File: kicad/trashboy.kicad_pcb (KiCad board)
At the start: 2 copper layers, 8 parts, among them J1 Conn_01x02, X1 TERMBLOCK_1X2

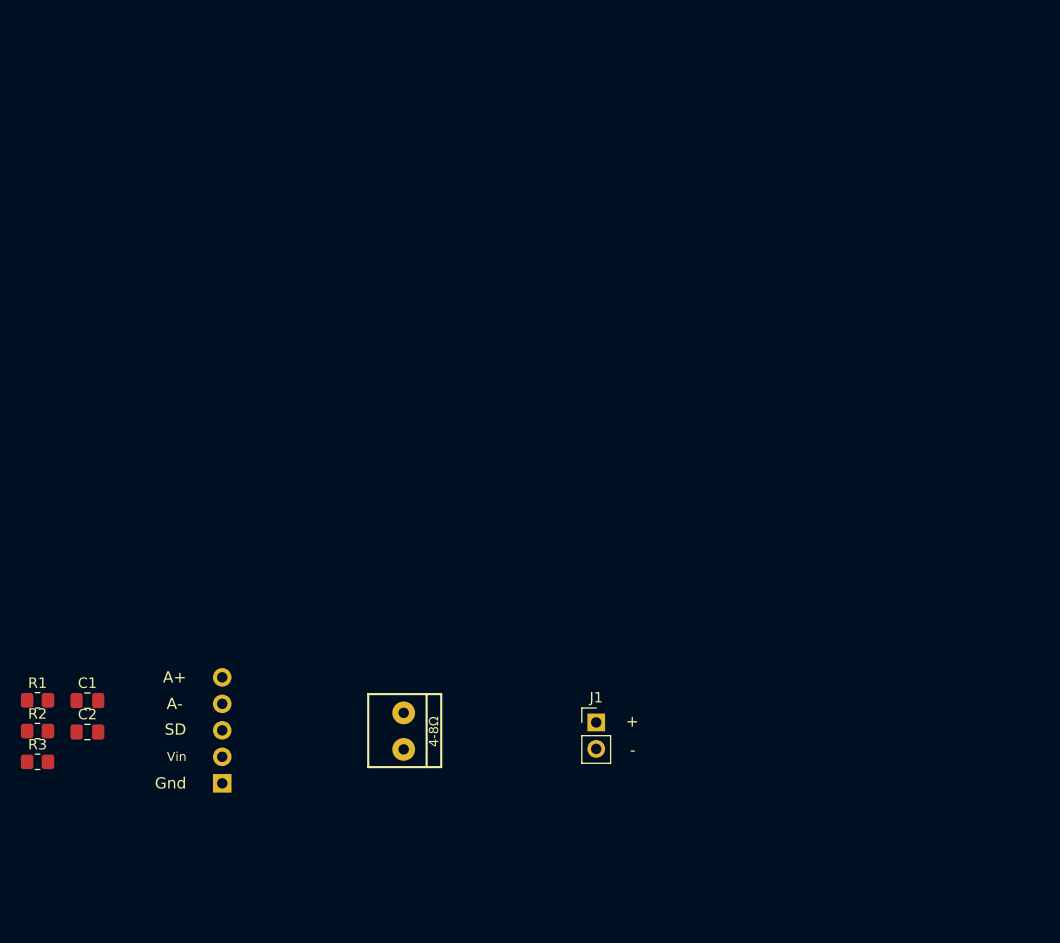
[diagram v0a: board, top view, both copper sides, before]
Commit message: Adding all of the component to the schematics.
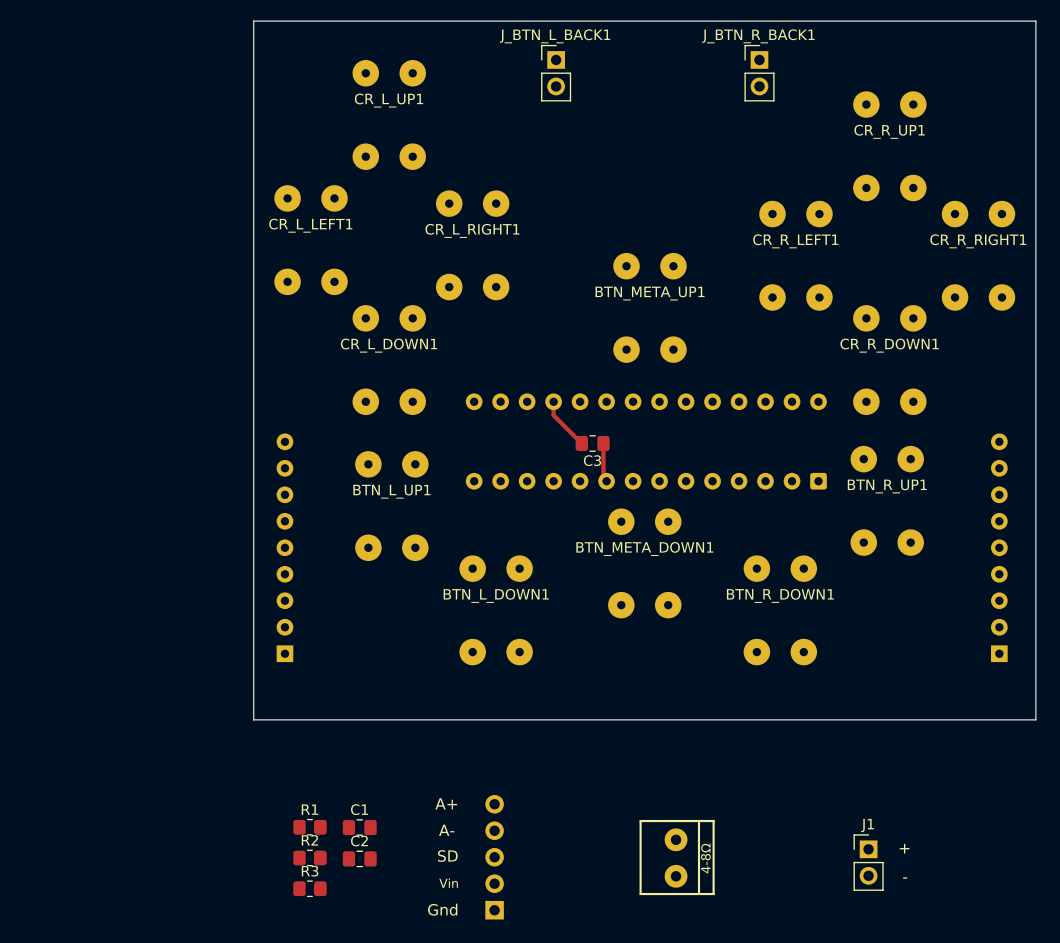
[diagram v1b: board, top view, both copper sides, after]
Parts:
- added BTN_L_DOWN1: SW_Push_Dual, buttons:SW_Push_Silicone_8x5mm, F.Cu at (165.8, 93.5)
- added BTN_L_UP1: SW_Push_Dual, buttons:SW_Push_Silicone_8x5mm, F.Cu at (155.8, 83.5)
- added BTN_META_DOWN1: SW_Push_Dual, buttons:SW_Push_Silicone_8x5mm, F.Cu at (180.0, 89.0)
- added BTN_META_UP1: SW_Push_Dual, buttons:SW_Push_Silicone_8x5mm, F.Cu at (180.5, 64.5)
- added BTN_R_DOWN1: SW_Push_Dual, buttons:SW_Push_Silicone_8x5mm, F.Cu at (193.0, 93.5)
- added BTN_R_UP1: SW_Push_Dual, buttons:SW_Push_Silicone_8x5mm, F.Cu at (203.2, 83.0)
- added C3: 10nF, Capacitor_SMD:C_0805_2012Metric_Pad1.18x1.45mm_HandSolder, F.Cu at (175.0, 77.5)
- added CR_L_DOWN1: SW_Push_Dual, buttons:SW_Push_Silicone_8x5mm, F.Cu at (155.5, 69.5)
- added CR_L_LEFT1: SW_Push_Dual, buttons:SW_Push_Silicone_8x5mm, F.Cu at (148.0, 58.0)
- added CR_L_RIGHT1: SW_Push_Dual, buttons:SW_Push_Silicone_8x5mm, F.Cu at (163.5, 58.5)
- added CR_L_UP1: SW_Push_Dual, buttons:SW_Push_Silicone_8x5mm, F.Cu at (155.5, 46.0)
- added CR_R_DOWN1: SW_Push_Dual, buttons:SW_Push_Silicone_8x5mm, F.Cu at (203.5, 69.5)
- added CR_R_LEFT1: SW_Push_Dual, buttons:SW_Push_Silicone_8x5mm, F.Cu at (194.5, 59.5)
- added CR_R_RIGHT1: SW_Push_Dual, buttons:SW_Push_Silicone_8x5mm, F.Cu at (212.0, 59.5)
- added CR_R_UP1: SW_Push_Dual, buttons:SW_Push_Silicone_8x5mm, F.Cu at (203.5, 49.0)
- added J_BTN_L_BACK1: Conn_01x02, Connector_PinHeader_2.54mm:PinHeader_1x02_P2.54mm_Vertical, F.Cu at (171.5, 40.7)
- added J_BTN_R_BACK1: Conn_01x02, Connector_PinHeader_2.54mm:PinHeader_1x02_P2.54mm_Vertical, F.Cu at (191.0, 40.7)
- added RN1: R_Network08_US, Resistor_THT:R_Array_SIP9, B.Cu at (145.5, 97.7)
- added RN2: R_Network08_US, Resistor_THT:R_Array_SIP9, B.Cu at (214.0, 97.7)
- added U1: MCP23017x-x-SP, Package_DIP:DIP-28_W7.62mm, B.Cu at (196.7, 81.1)
- moved J1 28.8 mm to (201.5, 116.4)
- moved C1 28.8 mm to (152.7, 114.3)
- moved C2 28.8 mm to (152.7, 117.3)
- moved JP1 28.8 mm to (165.6, 117.2)
- moved R1 28.8 mm to (147.9, 114.3)
- moved R2 28.8 mm to (147.9, 117.2)
- moved R3 28.8 mm to (147.9, 120.2)
- moved X1 28.8 mm to (183.0, 117.3)
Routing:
- net +3.3V: track 0.00 -> 5.12 mm
- net GND: track 0.00 -> 3.75 mm
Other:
- board outline added: 75 x 67 mm

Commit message: First attempt to place all the components, no traces yet.
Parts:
- added J3: Conn_01x06_Socket, Connector_PinHeader_2.54mm:PinHeader_1x06_P2.54mm_Vertical, B.Cu at (-15.9, -29.5)
- J1, JP1, J_BTN_L_BACK1, J_BTN_R_BACK1, X1: moved to B.Cu
- moved X1 236.0 mm to (-8.46, -20.7)
- moved J1 222.9 mm to (29.0, -24.8), turned to 180 degrees
- moved JP1 208.8 mm to (8.94, -20.8)
- moved C1 202.9 mm to (3.28, -23.0)
- moved C2 202.9 mm to (3.28, -20.0)
- moved R1 202.9 mm to (-1.50, -23.0)
- moved R2 202.9 mm to (-1.50, -20.1)
- moved R3 202.6 mm to (-1.39, -16.8)
- moved RN2 197.0 mm to (33.0, 20.0)
- moved CR_R_DOWN1 195.7 mm to (23.0, -6.00)
- moved CR_R_RIGHT1 195.4 mm to (31.0, -14.0)
- moved BTN_META_UP1 194.7 mm to (0.00, -8.50)
- moved RN1 194.7 mm to (-33.0, 20.0)
- moved BTN_L_DOWN1 194.6 mm to (-16.0, 24.0)
- moved BTN_R_UP1 194.5 mm to (23.0, 10.0)
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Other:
- outline, holes or cut-outs redrawn
- board text added: "TrashBoy v0.1 - June 2026 Sascha Häberling / Arno Puder"

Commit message: finished the PCB design and exported fabrication files.
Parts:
- removed J3: Conn_01x06_Socket, Connector_PinHeader_2.54mm:PinHeader_1x06_P2.54mm_Vertical
- added J2: Conn_01x07_Socket, Connector_PinHeader_2.54mm:PinHeader_1x07_P2.54mm_Vertical, B.Cu at (7.62, -31.0)
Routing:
- net GND: track 3.75 -> 257.2 mm
- net +3V3: track 0.00 -> 116.4 mm, vias 0 -> 1
- net SW1: track 0.00 -> 93.9 mm
- net SW2: track 0.00 -> 79.6 mm
- net SW4: track 0.00 -> 73.5 mm
- net SW6: track 0.00 -> 69.4 mm, vias 0 -> 1
- net SW0: track 0.00 -> 66.7 mm
- net SW7: track 0.00 -> 65.8 mm
- net SW3: track 0.00 -> 63.7 mm, vias 0 -> 1
- net SW10: track 0.00 -> 60.5 mm
- net +3.3V: track 5.12 -> 65.2 mm
- net SW9: track 0.00 -> 56.2 mm
- net SW12: track 0.00 -> 53.4 mm, vias 0 -> 1
- net SW11: track 0.00 -> 53.1 mm
- net SW14: track 0.00 -> 51.7 mm
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- added copper zone on B.Cu, net GND
- added copper zone on F.Cu, net GND
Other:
- board text added: "GND 3V SC SA IA IB SND"
